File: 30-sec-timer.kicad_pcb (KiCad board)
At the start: 2 copper layers, 53.3 x 52.1 mm, 25 parts, among them P1 6.3V AC IN, P2 CL12345, P3 Right, P4 Left, Q1 BC557, Q2 BC547, U1 LM7805CT, U2 LM555N

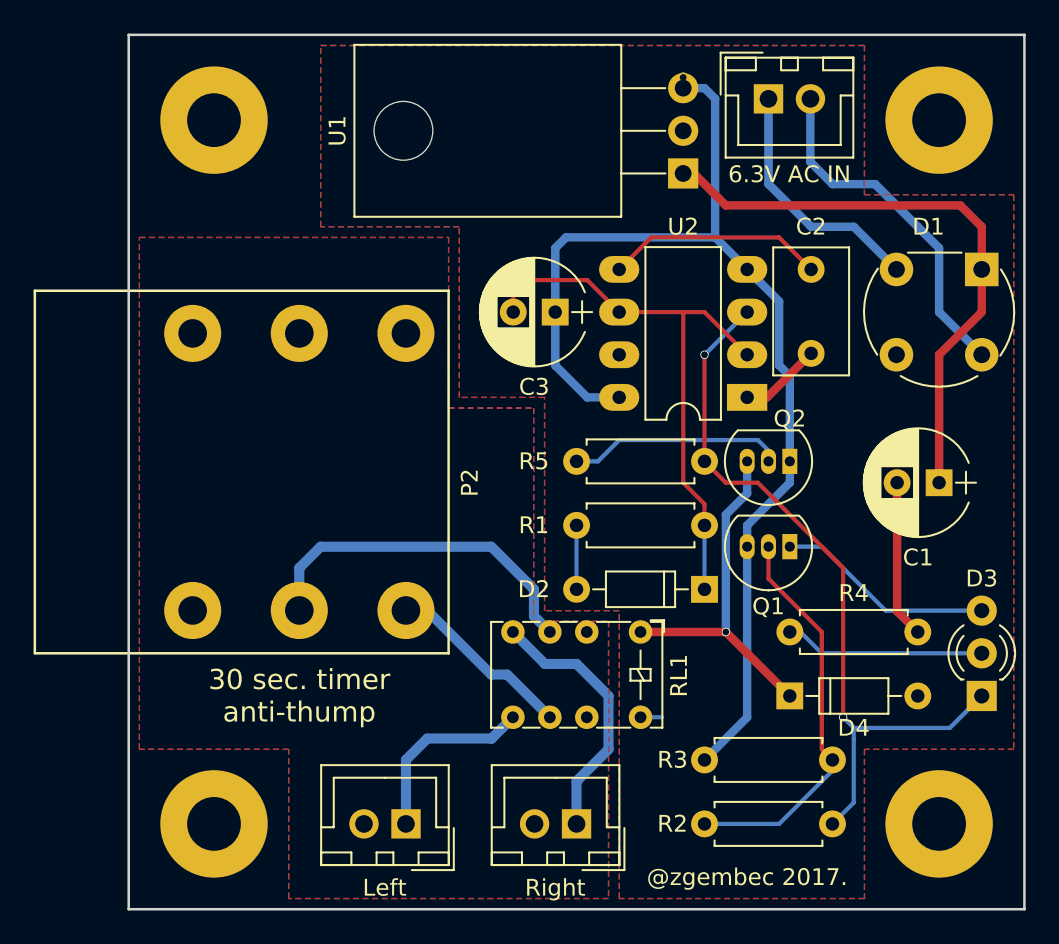
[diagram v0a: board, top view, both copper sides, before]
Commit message: 7805 mounting hole fix
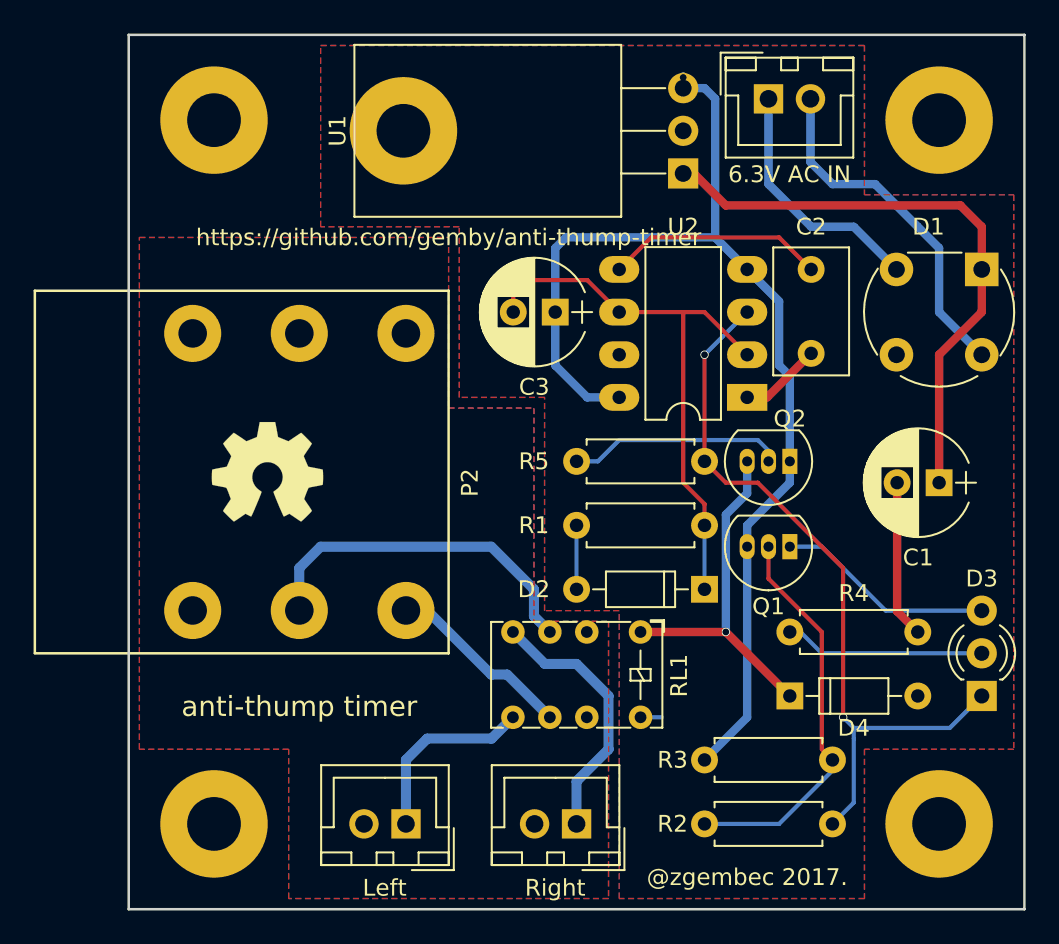
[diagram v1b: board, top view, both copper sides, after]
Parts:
- added REF***: OSHW-Symbol_6.7x6mm_SilkScreen, Symbols:OSHW-Symbol_6.7x6mm_SilkScreen, F.Cu at (150.5, 107.3)
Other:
- board text added: "anti-thump timer"
- board text added: "https://github.com/gemby/anti-thump-timer"
- board text removed: "30 sec. timer anti-thump"
